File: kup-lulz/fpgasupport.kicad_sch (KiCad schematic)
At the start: 44 parts, among them J5 JUMPER_0402, J6 XILINX_JTAG, U10 MT25QU256ABA8E12-0AUT, U9 XILINX_ULTRASCALEPLUS_B676

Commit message: Continued initial work on kup-lulz devboard
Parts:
- added C118, C119, C120, C121, C122, C123: 0.47 uF, azonenberg_pcb:EIA_0402_CAP_NOSILK, symbol device:C
- added R89, R90, R91: 4.7K, azonenberg_pcb:EIA_0402_RES_NOSILK, symbol device:R
- added U11, U12, U13: 74LVC1T45, azonenberg_pcb:DFN_6_0.5MM_1.6x1.6MM_TI_DPK, symbol special-azonenberg:74LVC1T45
- C59: footprint (none) -> azonenberg_pcb:EIA_0603_CAP_NOSILK
- C60: footprint (none) -> azonenberg_pcb:EIA_0402_CAP_NOSILK
- J5: footprint (none) -> azonenberg_pcb:EIA_0402_JUMPER
- J6: footprint (none) -> azonenberg_pcb:XILINX_JTAG_PTH_MOLEX_0878311420
- R40, R41, R42, R43, R44, R45, R46, R47, R48, R49, R50, R51, R52, R53, R54, R55, R56, R57, R58, R59: footprint (none) -> azonenberg_pcb:EIA_0402_RES_NOSILK
- U10: footprint (none) -> azonenberg_pcb:BGA_24_6x8_DEPOP1_1MM
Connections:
- net 1V8: now also C118.1, C119.1, C120.1, R89.2, R90.2, R91.2, U11.1 (VCCA), U11.5 (DIR), U12.1 (VCCA), U12.5 (DIR), U13.1 (VCCA)
- net 3V3: now also C121.1, C122.1, C123.1, U11.6 (VCCB), U12.6 (VCCB), U13.6 (VCCB)
- net FPGA_DONE: now also R90.1, U12.3 (A)
- net FPGA_INIT: now also R89.1, U11.3 (A)
- net FPGA_RESET_N: now also R91.1, U13.3 (A)
- net GND: now also C118.2, C119.2, C120.2, C121.2, C122.2, C123.2, U11.2 (GND), U12.2 (GND), U13.2 (GND), U13.5 (DIR)
- new net FPGA_DONE_3V3: U12.4 (B)
- new net FPGA_INIT_3V3: U11.4 (B)
- new net FPGA_RESET_N_3V3: U13.4 (B)
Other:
- note added: "We don't support holding DONE low to delay configuration It's only used as an output in this design"
- note removed: "TODO: FPGA_INIT, FPGA_DONE, FPGA_RESET level shift"

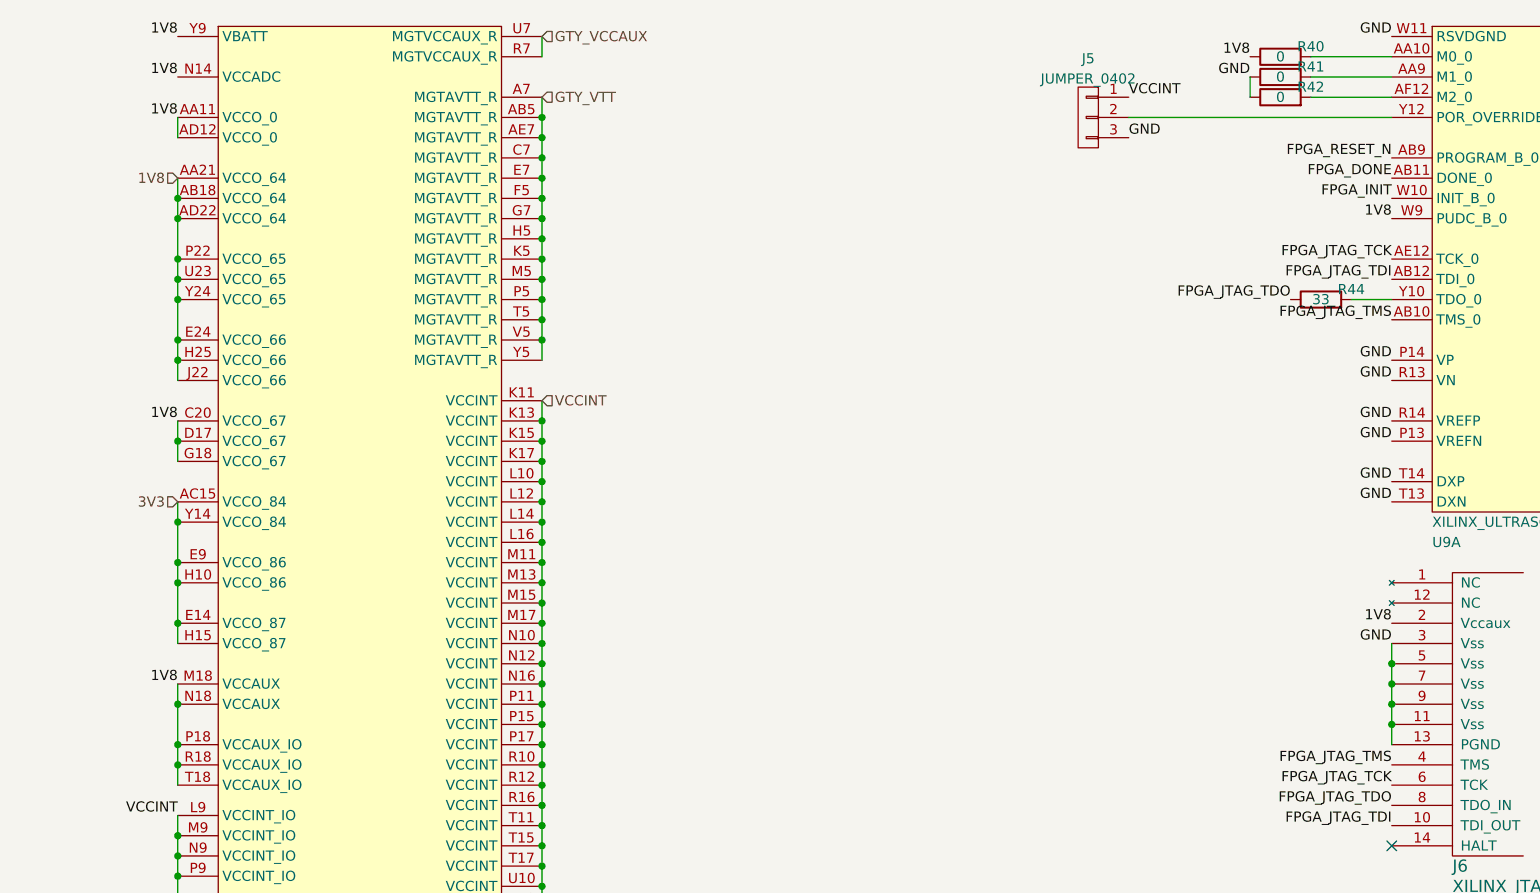
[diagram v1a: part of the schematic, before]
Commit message: Continued initial layout of kup-lulz
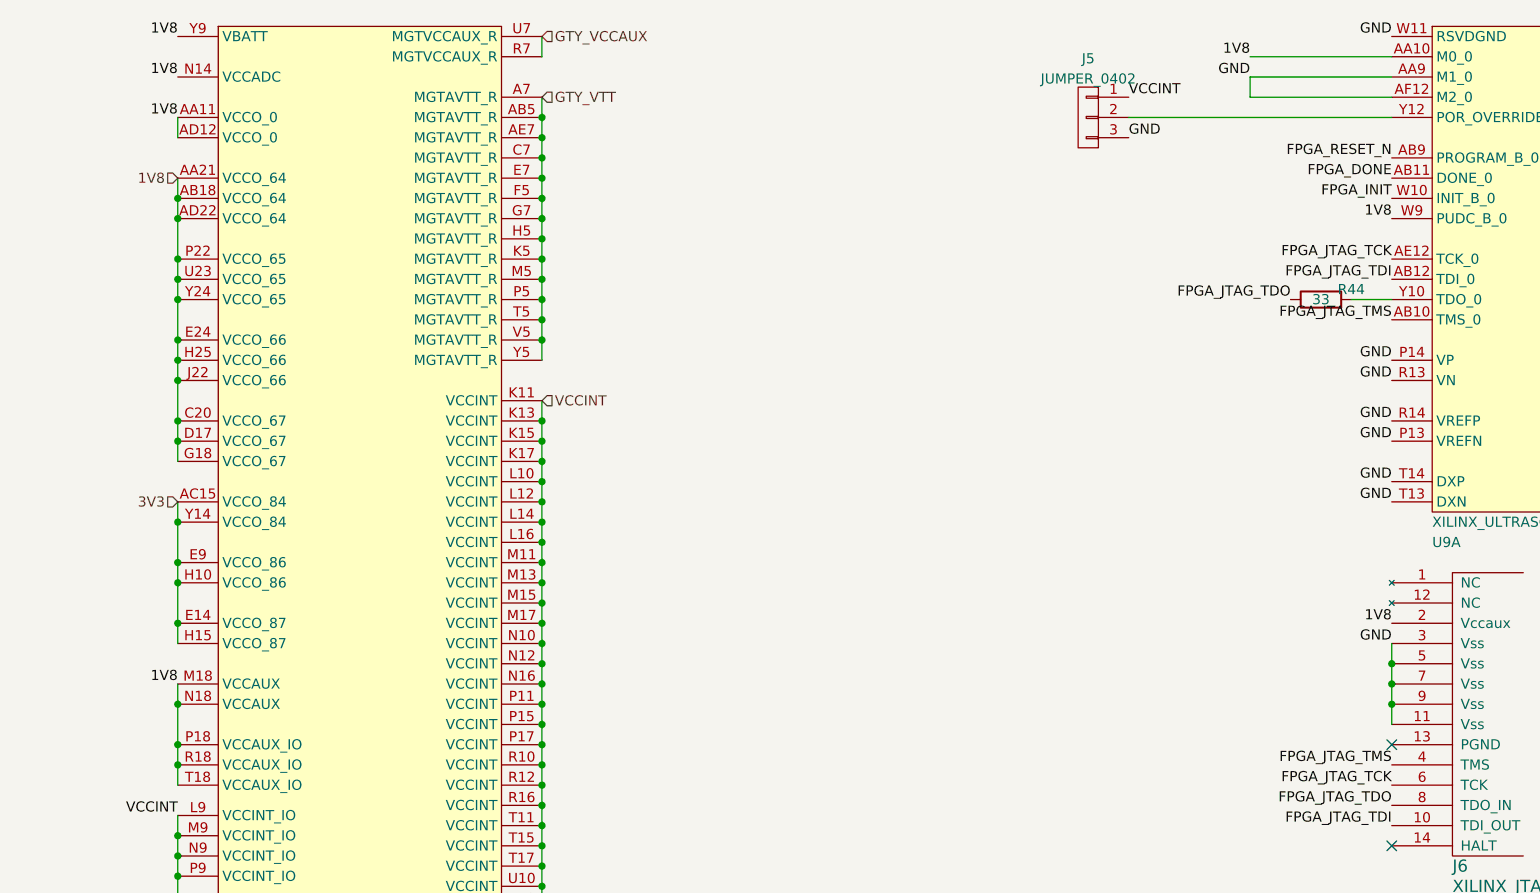
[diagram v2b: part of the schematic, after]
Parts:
- removed R40, R41, R42: 0, azonenberg_pcb:EIA_0402_RES_NOSILK, symbol device:R
- C111, C47, C48, C49, C50, C52, C58: footprint (none) -> azonenberg_pcb:EIA_0805_CAP_NOSILK
- C42, C43, C44, C45, C46, C51, C53, C54, C55, C56, C57: footprint (none) -> azonenberg_pcb:EIA_1210_CAP_NOSILK
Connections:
- net 1V8: now also U9.AA10 (M0_0)
- net GND: now also U9.AA9 (M1_0), U9.AF12 (M2_0); no longer J6.13 (PGND)
- no-connect marks 1 -> 2
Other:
- company: (none) -> Antikernel Labs
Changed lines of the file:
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@@
   (title_block
     (title "Kintex Ultrascale+ OshPark For The Lulz")
-    (date "2024-02-01")
+    (date "2024-02-05")
     (rev "0.1")
+    (company "Antikernel Labs")
+    (comment 1 "Andrew D. Zonenberg")
   )
   (junction (at 165.1 102.87) (diameter 0) (color 0 0 0 0)
@@
   (junction (at 210.82 49.53) (diameter 0) (color 0 0 0 0)
   )
+  (junction (at 165.1 62.23) (diameter 0) (color 0 0 0 0)
+  )
   (junction (at 90.17 43.18) (diameter 0) (color 0 0 0 0)
   )
@@
   (junction (at 222.25 228.6) (diameter 0) (color 0 0 0 0)
   )
-  (junction (at 317.5 105.41) (diameter 0) (color 0 0 0 0)
-  )
   (junction (at 165.1 69.85) (diameter 0) (color 0 0 0 0)
   )
@@
   (junction (at 67.31 76.2) (diameter 0) (color 0 0 0 0)
   )
+  (junction (at 165.1 67.31) (diameter 0) (color 0 0 0 0)
+  )
   (junction (at 24.13 40.64) (diameter 0) (color 0 0 0 0)
   )
@@
   )
   (no_connect (at 317.5 120.65))
+  (no_connect (at 317.5 107.95))
   (wire (pts (xy 210.82 115.57) (xy 210.82 118.11))
     (stroke (width 0) (type default) (color 0 0 0 0))
@@
     (stroke (width 0) (type default) (color 0 0 0 0))
   )
-  (wire (pts (xy 307.34 24.13) (xy 317.5 24.13))
+  (wire (pts (xy 299.72 24.13) (xy 317.5 24.13))
     (stroke (width 0) (type default) (color 0 0 0 0))
   )
@@
     (stroke (width 0) (type default) (color 0 0 0 0))
   )
+  (wire (pts (xy 165.1 62.23) (xy 165.1 67.31))
+    (stroke (width 0) (type default) (color 0 0 0 0))
+  )
   (wire (pts (xy 210.82 85.09) (xy 210.82 87.63))
     (stroke (width 0) (type default) (color 0 0 0 0))
@@
     (stroke (width 0) (type default) (color 0 0 0 0))
   )
-  (wire (pts (xy 317.5 105.41) (xy 317.5 107.95))
-    (stroke (width 0) (type default) (color 0 0 0 0))
-  )
   (wire (pts (xy 67.31 149.86) (xy 67.31 152.4))
     (stroke (width 0) (type default) (color 0 0 0 0))
@@
     (stroke (width 0) (type default) (color 0 0 0 0))
   )
-  (wire (pts (xy 307.34 26.67) (xy 317.5 26.67))
+  (wire (pts (xy 299.72 26.67) (xy 317.5 26.67))
     (stroke (width 0) (type default) (color 0 0 0 0))
   )
@@
     (stroke (width 0) (type default) (color 0 0 0 0))
   )
-  (wire (pts (xy 307.34 21.59) (xy 317.5 21.59))
+  (wire (pts (xy 299.72 21.59) (xy 317.5 21.59))
     (stroke (width 0) (type default) (color 0 0 0 0))
   )
@@
     (effects (font (size 1.27 1.27)) (justify right bottom))
   )
-  (label "1V8" (at 165.1 67.31 180)
-    (effects (font (size 1.27 1.27)) (justify right bottom))
-  )
   (label "1V8" (at 299.72 21.59 180)
     (effects (font (size 1.27 1.27)) (justify right bottom))
@@
     (pin "2")
   )
-  (symbol (lib_id "device:R") (at 303.53 24.13 90) (unit 1)
-    (in_bom yes) (on_board yes)
-    (property "Reference" "R41" (id 0) (at 307.34 22.86 90))
-    (property "Value" "0" (id 1) (at 303.53 24.13 90))
-    (property "Footprint" "azonenberg_pcb:EIA_0402_RES_NOSILK" (id 2) (at 303.53 25.908 90)
-      (effects (font (size 1.27 1.27)) hide)
-    )
-    (property "Datasheet" "" (id 3) (at 303.53 24.13 0)
-      (effects (font (size 1.27 1.27)) hide)
-    )
-    (pin "1")
-    (pin "2")
-  )
   (symbol (lib_id "device:C") (at 29.21 193.04 0) (unit 1)
     (in_bom yes) (on_board yes) (fields_autoplaced)
@@
       (effects (font (size 1.27 1.27)) (justify left))
     )
-    (property "Footprint" "" (id 2) (at 30.1752 196.85 0)
+    (property "Footprint" "azonenberg_pcb:EIA_1210_CAP_NOSILK" (id 2) (at 30.1752 196.85 0)
       (effects (font (size 1.27 1.27)) hide)
     )
@@
       (effects (font (size 1.27 1.27)) (justify left))
     )
-    (property "Footprint" "" (id 2) (at 30.1752 266.7 0)
+    (property "Footprint" "azonenberg_pcb:EIA_1210_CAP_NOSILK" (id 2) (at 30.1752 266.7 0)
       (effects (font (size 1.27 1.27)) hide)
     )
@@
       (effects (font (size 1.27 1.27)) (justify left))
     )
-    (property "Footprint" "" (id 2) (at 69.5452 180.34 0)
+    (property "Footprint" "azonenberg_pcb:EIA_1210_CAP_NOSILK" (id 2) (at 69.5452 180.34 0)
       (effects (font (size 1.27 1.27)) hide)
     )
@@
       (effects (font (size 1.27 1.27)) (justify left))
     )
-    (property "Footprint" "" (id 2) (at 30.1752 213.36 0)
+    (property "Footprint" "azonenberg_pcb:EIA_1210_CAP_NOSILK" (id 2) (at 30.1752 213.36 0)
       (effects (font (size 1.27 1.27)) hide)
     )
@@
       (effects (font (size 1.27 1.27)) (justify left))
     )
-    (property "Footprint" "" (id 2) (at 41.6052 213.36 0)
+    (property "Footprint" "azonenberg_pcb:EIA_0805_CAP_NOSILK" (id 2) (at 41.6052 213.36 0)
       (effects (font (size 1.27 1.27)) hide)
     )
@@
       (effects (font (size 1.27 1.27)) (justify left))
     )
-    (property "Footprint" "" (id 2) (at 94.9452 180.34 0)
+    (property "Footprint" "azonenberg_pcb:EIA_1210_CAP_NOSILK" (id 2) (at 94.9452 180.34 0)
       (effects (font (size 1.27 1.27)) hide)
     )
@@
       (effects (font (size 1.27 1.27)) (justify left))
     )
-    (property "Footprint" "" (id 2) (at 54.3052 266.7 0)
+    (property "Footprint" "azonenberg_pcb:EIA_0805_CAP_NOSILK" (id 2) (at 54.3052 266.7 0)
       (effects (font (size 1.27 1.27)) hide)
     )
@@
       (effects (font (size 1.27 1.27)) (justify left))
     )
-    (property "Footprint" "" (id 2) (at 30.1752 180.34 0)
+    (property "Footprint" "azonenberg_pcb:EIA_1210_CAP_NOSILK" (id 2) (at 30.1752 180.34 0)
       (effects (font (size 1.27 1.27)) hide)
     )
@@
       (effects (font (size 1.27 1.27)) (justify left))
     )
-    (property "Footprint" "" (id 2) (at 82.2452 180.34 0)
+    (property "Footprint" "azonenberg_pcb:EIA_1210_CAP_NOSILK" (id 2) (at 82.2452 180.34 0)
       (effects (font (size 1.27 1.27)) hide)
     )
@@
       (effects (font (size 1.27 1.27)) (justify left))
     )
-    (property "Footprint" "" (id 2) (at 41.6052 266.7 0)
+    (property "Footprint" "azonenberg_pcb:EIA_0805_CAP_NOSILK" (id 2) (at 41.6052 266.7 0)
       (effects (font (size 1.27 1.27)) hide)
     )
@@
       (effects (font (size 1.27 1.27)) (justify left))
     )
-    (property "Footprint" "" (id 2) (at 41.6052 241.3 0)
+    (property "Footprint" "azonenberg_pcb:EIA_0805_CAP_NOSILK" (id 2) (at 41.6052 241.3 0)
       (effects (font (size 1.27 1.27)) hide)
     )
@@
       (effects (font (size 1.27 1.27)) (justify left))
     )
-    (property "Footprint" "" (id 2) (at 56.8452 180.34 0)
+    (property "Footprint" "azonenberg_pcb:EIA_1210_CAP_NOSILK" (id 2) (at 56.8452 180.34 0)
       (effects (font (size 1.27 1.27)) hide)
     )
@@
       (effects (font (size 1.27 1.27)) (justify left))
     )
-    (property "Footprint" "" (id 2) (at 107.6452 180.34 0)
+    (property "Footprint" "azonenberg_pcb:EIA_1210_CAP_NOSILK" (id 2) (at 107.6452 180.34 0)
       (effects (font (size 1.27 1.27)) hide)
     )
@@
       (effects (font (size 1.27 1.27)) (justify left))
     )
-    (property "Footprint" "" (id 2) (at 119.0752 180.34 0)
+    (property "Footprint" "azonenberg_pcb:EIA_0805_CAP_NOSILK" (id 2) (at 119.0752 180.34 0)
       (effects (font (size 1.27 1.27)) hide)
     )
@@
       (effects (font (size 1.27 1.27)) (justify left))
     )
-    (property "Footprint" "" (id 2) (at 54.3052 241.3 0)
+    (property "Footprint" "azonenberg_pcb:EIA_0805_CAP_NOSILK" (id 2) (at 54.3052 241.3 0)
       (effects (font (size 1.27 1.27)) hide)
     )
@@
     (pin "2")
   )
-  (symbol (lib_id "device:R") (at 303.53 21.59 90) (unit 1)
-    (in_bom yes) (on_board yes)
-    (property "Reference" "R40" (id 0) (at 307.34 20.32 90))
-    (property "Value" "0" (id 1) (at 303.53 21.59 90))
-    (property "Footprint" "azonenberg_pcb:EIA_0402_RES_NOSILK" (id 2) (at 303.53 23.368 90)
-      (effects (font (size 1.27 1.27)) hide)
-    )
-    (property "Datasheet" "" (id 3) (at 303.53 21.59 0)
-      (effects (font (size 1.27 1.27)) hide)
-    )
-    (pin "1")
-    (pin "2")
-  )
-  (symbol (lib_id "device:R") (at 303.53 26.67 90) (unit 1)
-    (in_bom yes) (on_board yes)
-    (property "Reference" "R42" (id 0) (at 307.34 25.4 90))
-    (property "Value" "0" (id 1) (at 303.53 26.67 90))
-    (property "Footprint" "azonenberg_pcb:EIA_0402_RES_NOSILK" (id 2) (at 303.53 28.448 90)
-      (effects (font (size 1.27 1.27)) hide)
-    )
-    (property "Datasheet" "" (id 3) (at 303.53 26.67 0)
-      (effects (font (size 1.27 1.27)) hide)
-    )
-    (pin "1")
-    (pin "2")
-  )
   (symbol (lib_id "device:C") (at 29.21 237.49 0) (unit 1)
     (in_bom yes) (on_board yes) (fields_autoplaced)
@@
       (effects (font (size 1.27 1.27)) (justify left))
     )
-    (property "Footprint" "" (id 2) (at 30.1752 241.3 0)
+    (property "Footprint" "azonenberg_pcb:EIA_1210_CAP_NOSILK" (id 2) (at 30.1752 241.3 0)
       (effects (font (size 1.27 1.27)) hide)
     )
@@
       (effects (font (size 1.27 1.27)) (justify left))
     )
-    (property "Footprint" "" (id 2) (at 44.1452 180.34 0)
+    (property "Footprint" "azonenberg_pcb:EIA_1210_CAP_NOSILK" (id 2) (at 44.1452 180.34 0)
       (effects (font (size 1.27 1.27)) hide)
     )
@@
       (effects (font (size 1.27 1.27)) (justify left))
     )
-    (property "Footprint" "" (id 2) (at 41.6052 196.85 0)
+    (property "Footprint" "azonenberg_pcb:EIA_0805_CAP_NOSILK" (id 2) (at 41.6052 196.85 0)
       (effects (font (size 1.27 1.27)) hide)
     )

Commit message: Continued initial layout
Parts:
- removed R58, R59: 4.7K, azonenberg_pcb:EIA_0402_RES_NOSILK, symbol device:R
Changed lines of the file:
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@@
   (junction (at 90.17 127) (diameter 0) (color 0 0 0 0)
   )
-  (junction (at 378.46 90.17) (diameter 0) (color 0 0 0 0)
-  )
   (junction (at 165.1 92.71) (diameter 0) (color 0 0 0 0)
   )
@@
   (junction (at 133.35 68.58) (diameter 0) (color 0 0 0 0)
   )
-  (junction (at 378.46 92.71) (diameter 0) (color 0 0 0 0)
-  )
   (junction (at 24.13 121.92) (diameter 0) (color 0 0 0 0)
   )
@@
     (stroke (width 0) (type default) (color 0 0 0 0))
   )
-  (wire (pts (xy 374.65 95.25) (xy 378.46 95.25))
-    (stroke (width 0) (type default) (color 0 0 0 0))
-  )
   (wire (pts (xy 165.1 121.92) (xy 165.1 124.46))
     (stroke (width 0) (type default) (color 0 0 0 0))
@@
     (stroke (width 0) (type default) (color 0 0 0 0))
   )
-  (wire (pts (xy 378.46 95.25) (xy 378.46 92.71))
-    (stroke (width 0) (type default) (color 0 0 0 0))
-  )
   (wire (pts (xy 24.13 43.18) (xy 24.13 45.72))
     (stroke (width 0) (type default) (color 0 0 0 0))
@@
     (stroke (width 0) (type default) (color 0 0 0 0))
   )
-  (wire (pts (xy 374.65 92.71) (xy 378.46 92.71))
-    (stroke (width 0) (type default) (color 0 0 0 0))
-  )
   (wire (pts (xy 24.13 149.86) (xy 24.13 152.4))
     (stroke (width 0) (type default) (color 0 0 0 0))
@@
     (stroke (width 0) (type default) (color 0 0 0 0))
   )
-  (wire (pts (xy 378.46 92.71) (xy 378.46 90.17))
-    (stroke (width 0) (type default) (color 0 0 0 0))
-  )
   (wire (pts (xy 90.17 119.38) (xy 90.17 121.92))
     (stroke (width 0) (type default) (color 0 0 0 0))
@@
     (effects (font (size 1.27 1.27)) (justify left bottom))
   )
-  (label "FPGA_INIT" (at 367.03 92.71 180)
-    (effects (font (size 1.27 1.27)) (justify right bottom))
-  )
   (label "VCCINT" (at 284.48 26.67 0)
     (effects (font (size 1.27 1.27)) (justify left bottom))
@@
     (effects (font (size 1.27 1.27)) (justify right bottom))
   )
-  (label "FPGA_DONE" (at 367.03 95.25 180)
-    (effects (font (size 1.27 1.27)) (justify right bottom))
-  )
   (label "1V8" (at 308.61 153.67 180)
     (effects (font (size 1.27 1.27)) (justify right bottom))
@@
     (pin "2")
   )
-  (symbol (lib_id "device:R") (at 370.84 95.25 90) (unit 1)
-    (in_bom yes) (on_board yes)
-    (property "Reference" "R59" (id 0) (at 374.65 93.98 90))
-    (property "Value" "4.7K" (id 1) (at 370.84 95.25 90))
-    (property "Footprint" "azonenberg_pcb:EIA_0402_RES_NOSILK" (id 2) (at 370.84 97.028 90)
-      (effects (font (size 1.27 1.27)) hide)
-    )
-    (property "Datasheet" "" (id 3) (at 370.84 95.25 0)
-      (effects (font (size 1.27 1.27)) hide)
-    )
-    (pin "1")
-    (pin "2")
-  )
   (symbol (lib_id "xilinx-azonenberg:XILINX_ULTRASCALEPLUS_B676") (at 29.21 156.21 0) (unit 2)
     (in_bom yes) (on_board yes)
@@
       (effects (font (size 1.27 1.27)) hide)
     )
-    (pin "1")
-    (pin "2")
-  )
-  (symbol (lib_id "device:R") (at 370.84 92.71 90) (unit 1)
-    (in_bom yes) (on_board yes)
-    (property "Reference" "R58" (id 0) (at 374.65 91.44 90))
-    (property "Value" "4.7K" (id 1) (at 370.84 92.71 90))
-    (property "Footprint" "azonenberg_pcb:EIA_0402_RES_NOSILK" (id 2) (at 370.84 94.488 90)
-      (effects (font (size 1.27 1.27)) hide)
-    )
-    (property "Datasheet" "" (id 3) (at 370.84 92.71 0)
-      (effects (font (size 1.27 1.27)) hide)
-    )
